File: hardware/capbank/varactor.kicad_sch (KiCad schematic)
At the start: 12 parts, among them U2 OPA2202IDR

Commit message: KiCad changes
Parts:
- R2: value 50k -> 110k
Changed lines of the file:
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@@
 			)
 		)
-		(property "Value" "50k"
+		(property "Value" "110k"
 			(at 81.28 66.04 90)
 			(effects

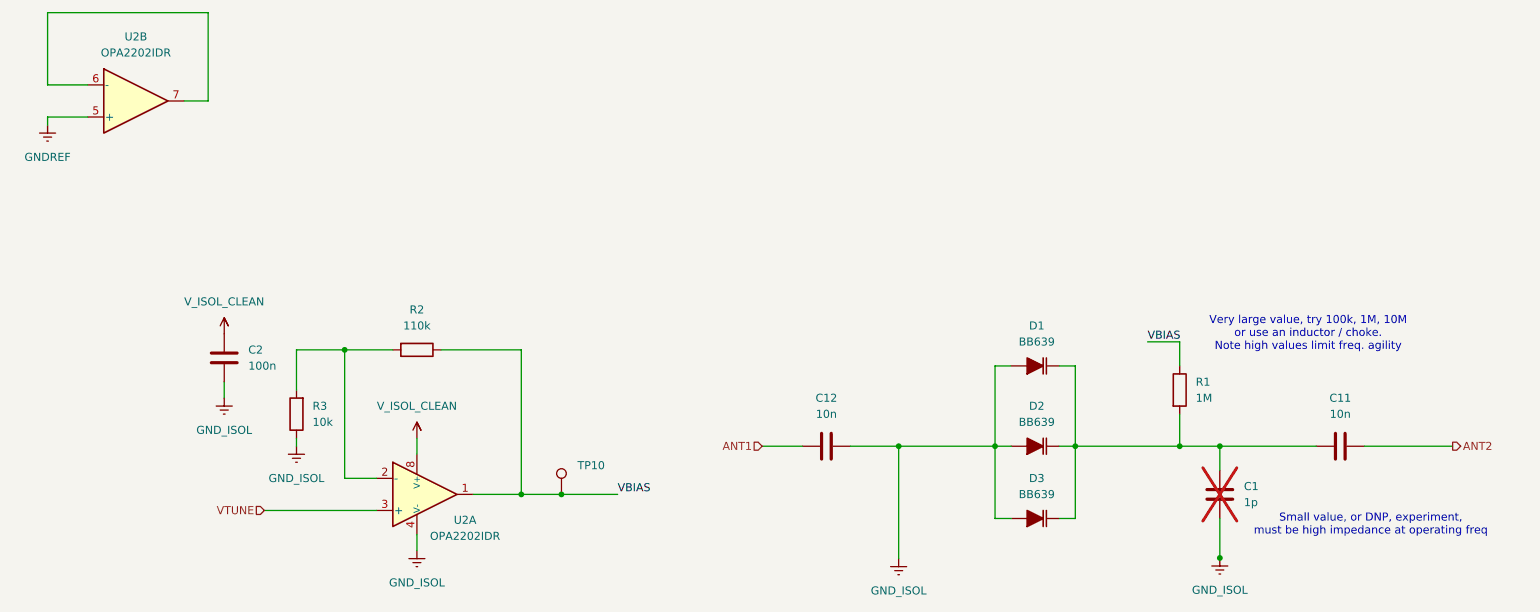
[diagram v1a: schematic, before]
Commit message: Progress, layout nearly completed, build oscillator on breadboard
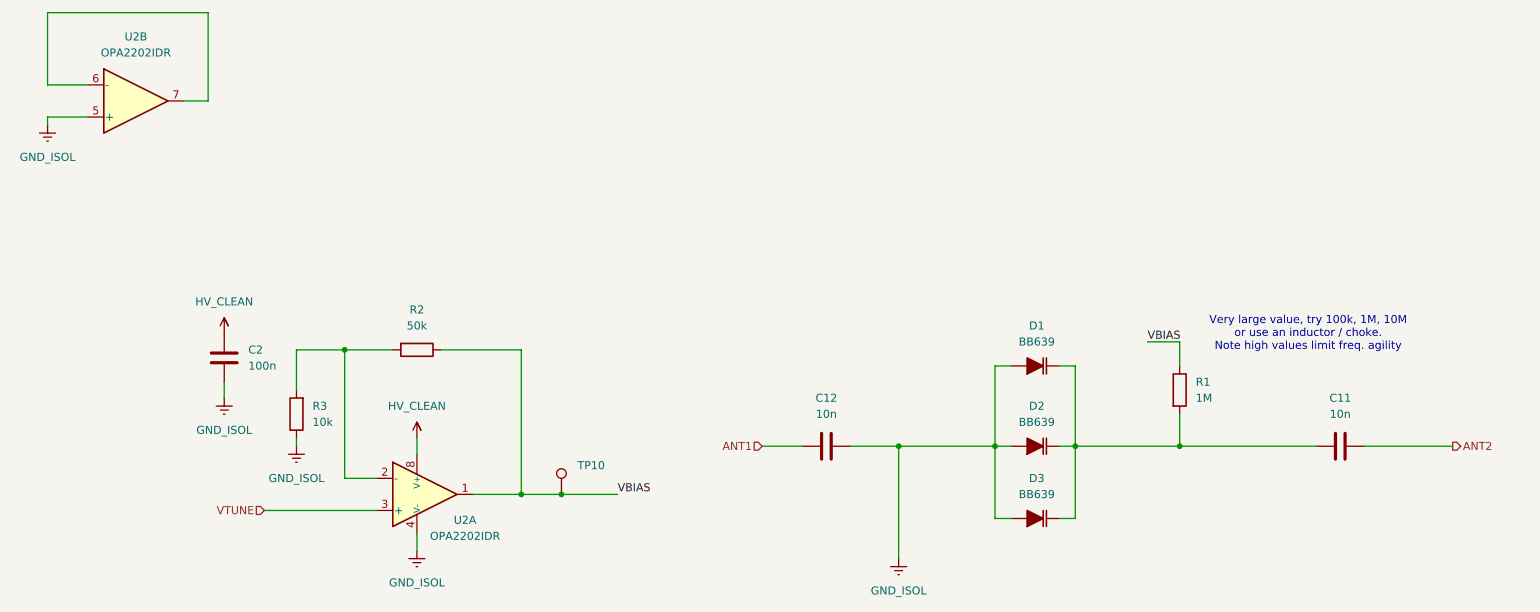
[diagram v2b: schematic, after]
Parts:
- removed C1: 1p, PCM_Capacitor_SMD_AKL:C_0603_1608Metric, symbol Device:C
- C11: footprint Capacitor_SMD:C_2220_5750Metric -> Capacitor_SMD:C_1206_3216Metric
- R2: value 110k -> 50k
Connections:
- net GNDREF is gone; now on net GND_ISOL: U2.5 (+)
- net V_ISOL_CLEAN renamed HV_CLEAN
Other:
- note removed: "Small value, or DNP, experiment, must be high impedance at operating freq"
